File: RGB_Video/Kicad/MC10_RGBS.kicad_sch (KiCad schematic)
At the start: 49 parts, among them J1 DIN-7, Q1 2N3904, Q10 BC558, Q11 2N3904, Q12 BC558, Q13 BC558, Q2 2N3904, Q3 2N3904, Q4 2N3904, Q5 2N3904, Q6 2N3904, Q7 2N3904, Q8 2N3904, Q9 2N3904

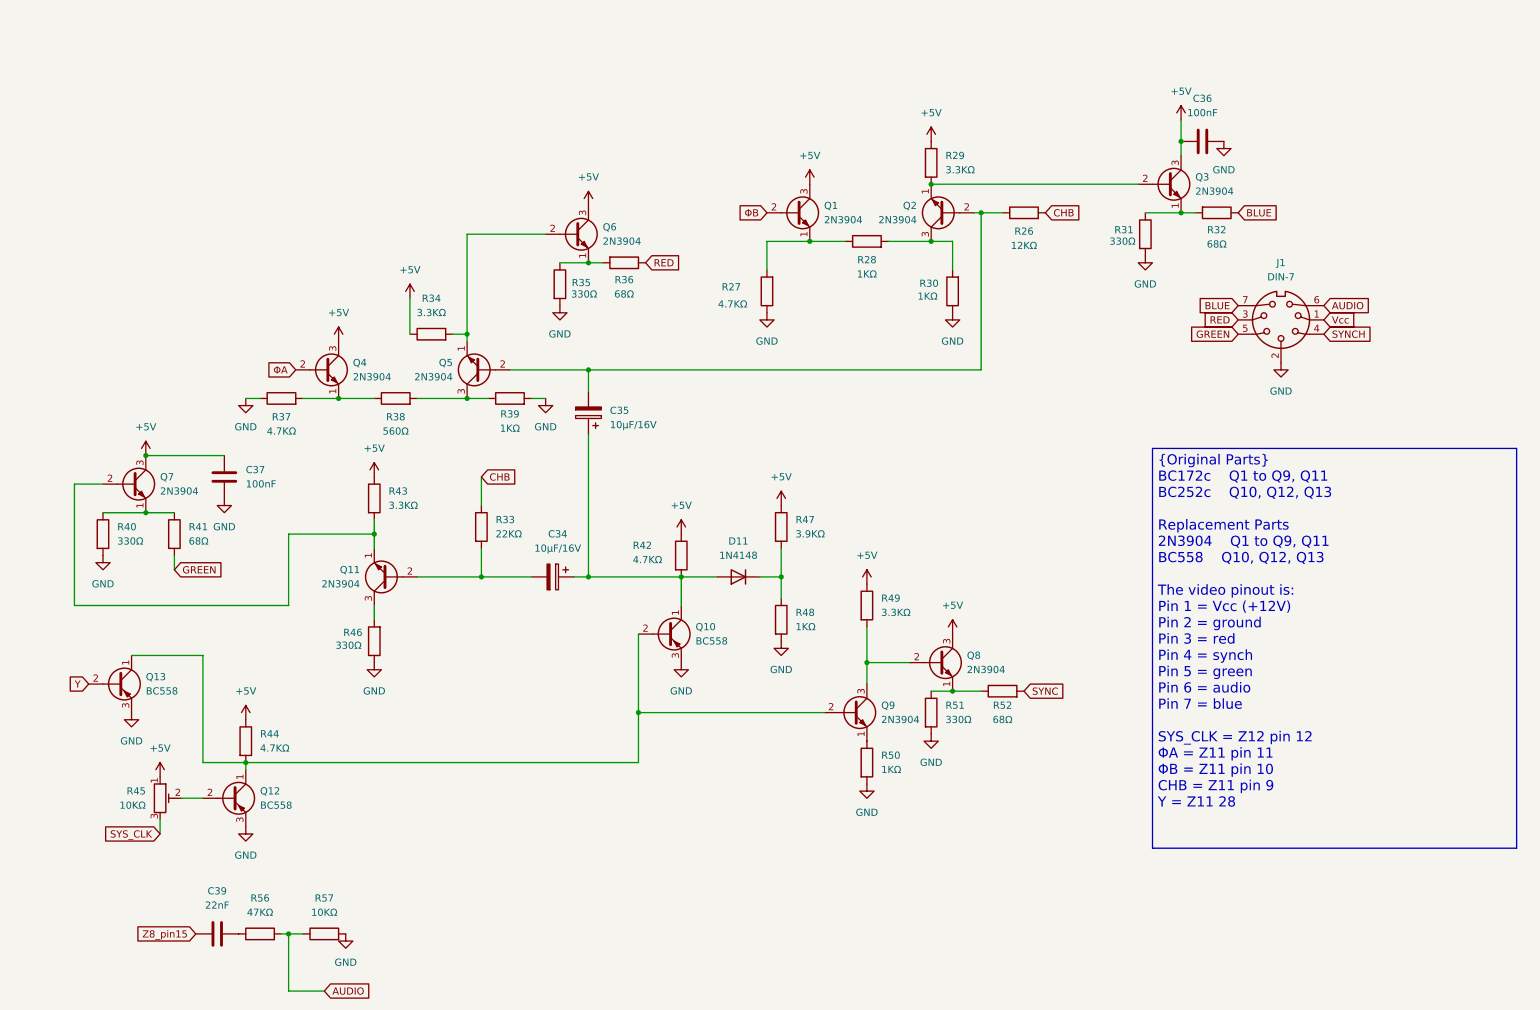
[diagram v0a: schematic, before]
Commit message: Added MC1372 for system clock generation
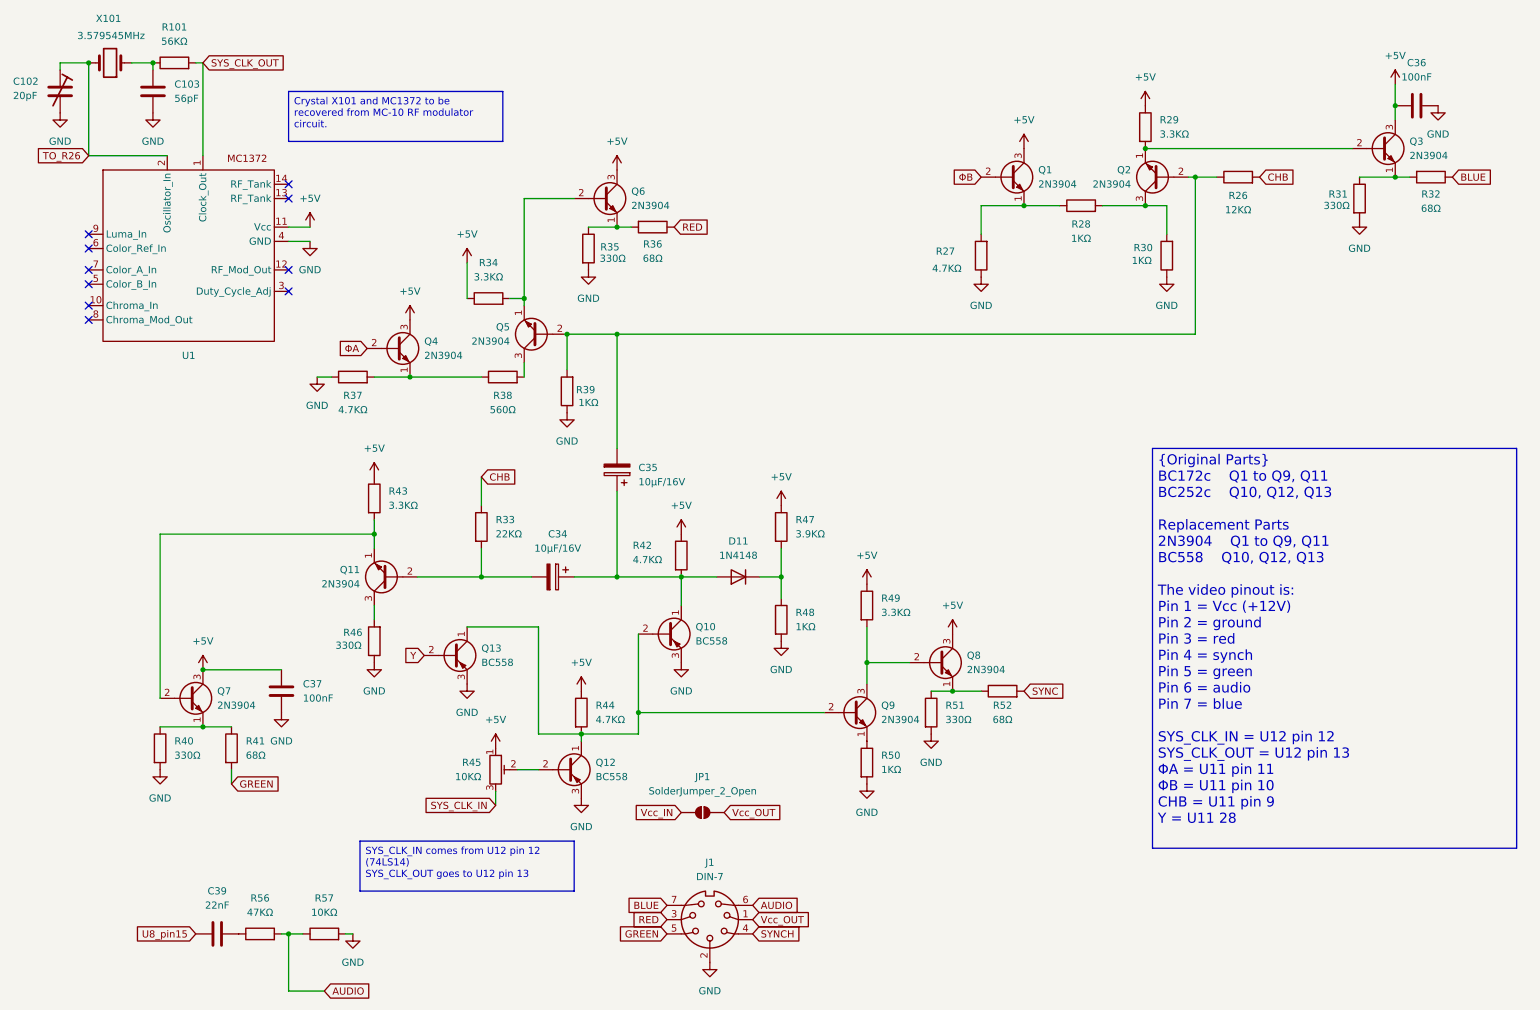
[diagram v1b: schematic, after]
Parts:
- added C102: 20pF, symbol Device:C_Trim
- added C103: 56pF, symbol Device:C
- added JP1: SolderJumper_2_Open, symbol Jumper:SolderJumper_2_Open
- added R101: 56KΩ, symbol Device:R
- added U1: ~, symbol Clueless_Engineer:MC1372
- added X101: 3.579545MHz, symbol Device:Crystal
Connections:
- net +5V: now also U1.11 (Vcc)
- net GND: now also R39.1, C102.2, C103.2, U1.4 (GND); no longer R39.2
- net at C35.2, Q2.2 (B), Q5.2 (B)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: now also R39.2
- net at Q5.3 (C), R38.2: no longer R39.1
- net SYS_CLK renamed SYS_CLK_IN
- net Vcc renamed Vcc_OUT
- net Vcc_OUT: now also JP1.2 (B)
- net Z8_pin15 renamed U8_pin15
- new net: C103.1, R101.1, X101.1
- new net SYS_CLK_OUT: R101.2, U1.1 (Clock_Out)
- new net TO_R26: C102.1, U1.2 (Oscillator_In), X101.2
- new net Vcc_IN: JP1.1 (A)
- no-connect marks 0 -> 10
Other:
- moved on the sheet: C35, C36, C37, J1, Q1, Q12, Q13, Q2, Q3, Q4, Q5, Q6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

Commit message: Changed transistor types
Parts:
- added J2: MC-10_Signals, Connector_PinSocket_2.54mm:PinSocket_1x09_P2.54mm_Vertical, symbol Connector_Generic:Conn_01x09
- added R1: 100KΩ, Resistor_SMD:R_0603_1608Metric_Pad0.98x0.95mm_HandSolder, symbol Device:R
- C102: footprint (none) -> Capacitor_SMD:C_Trimmer_Murata_TZB4-B
- C103, C36, C37, C39: footprint (none) -> Capacitor_THT:C_Disc_D3.0mm_W2.0mm_P2.50mm
- C34, C35: footprint (none) -> Capacitor_THT:CP_Radial_D5.0mm_P2.50mm
- D11: footprint Diode_THT:D_DO-35_SOD27_P7.62mm_Horizontal -> Diode_SMD:D_SOD-323_HandSoldering
- J1: value DIN-7 -> RGBS_Output; footprint (none) -> Connector_PinHeader_2.54mm:PinHeader_1x07_P2.54mm_Vertical
- JP1: value SolderJumper_2_Open -> 12V_to_DIN; footprint (none) -> Jumper:SolderJumper-2_P1.3mm_Open_Pad1.0x1.5mm
- Q1, Q11, Q2, Q3, Q4, Q5, Q6, Q7, Q8, Q9: value 2N3904 -> BC550C
- Q10, Q12, Q13: value BC558 -> BC559C
- R101, R26, R27, R28, R29, R30, R31, R32, R33, R34, R35, R36, R37, R38, R39, R40, R41, R42, R43, R44, R46, R47, R48, R49, R50, R51, R52, R56, R57: footprint (none) -> Resistor_SMD:R_0603_1608Metric_Pad0.98x0.95mm_HandSolder
- R45: footprint (none) -> Clueless_Engineer:PTN091V10115K1B
- U1: footprint (none) -> Package_DIP:DIP-14_W7.62mm
- X101: footprint (none) -> Crystal:Crystal_HC49-U_Vertical
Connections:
- net +5V: now also J2.1 (Pin_1), R1.1
- net AUDIO: now also R56.1, R57.2; no longer R56.2, R57.1
- net CHB: now also J2.8 (Pin_8)
- net GND: now also R57.1, J2.7 (Pin_7); no longer R57.2
- net SYS_CLK_IN: now also J2.2 (Pin_2)
- net SYS_CLK_OUT: now also J2.3 (Pin_3)
- net U8_pin15: now also C39.2; no longer C39.1
- net Vcc_IN: now also J2.6 (Pin_6)
- net Y: now also J2.9 (Pin_9)
- net ΦA: now also J2.4 (Pin_4)
- net ΦB: now also J2.5 (Pin_5)
- net TO_R26: no longer names the net of C102.1, U1.2 (Oscillator_In), X101.2
- net TO_R26: now also R1.2
- new net: C39.1, R56.2
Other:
- moved on the sheet: C36, C37, C39, J1, JP1, Q1, Q2, Q3, Q7, R26, R27, R28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
